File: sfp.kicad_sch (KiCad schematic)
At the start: 33 parts, among them J12 Bel-Fuse_SFP+_1x20_SS-79100-0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

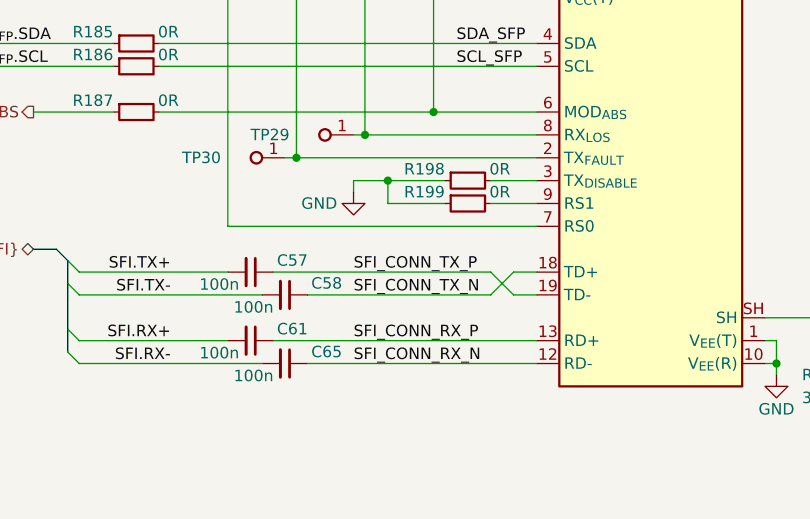
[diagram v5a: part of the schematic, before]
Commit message: [#85326] Update SFP connection
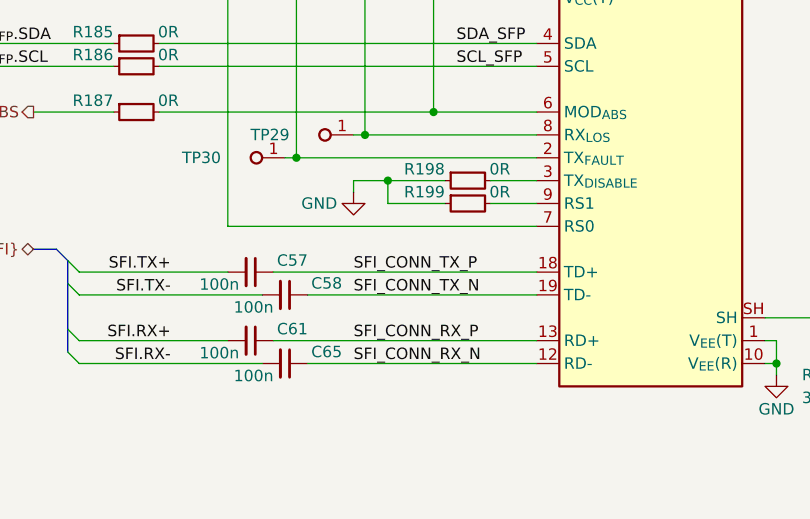
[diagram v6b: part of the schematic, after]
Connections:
- net SFI_CONN_TX_N: now also J12.19 (TD-); no longer J12.18 (TD+)
- net SFI_CONN_TX_P: now also J12.18 (TD+); no longer J12.19 (TD-)
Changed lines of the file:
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@@
-	(wire
-		(pts
-			(xy 182.88 151.13) (xy 185.42 151.13)
-		)
-		(stroke
-			(width 0)
-			(type default)
-		)
-	)
 	(wire
 		(pts
@@
 	(wire
 		(pts
-			(xy 182.88 153.67) (xy 185.42 153.67)
-		)
-		(stroke
-			(width 0)
-			(type default)
-		)
-	)
-	(wire
-		(pts
 			(xy 287.02 156.21) (xy 287.02 161.29)
 		)
@@
 	(wire
 		(pts
-			(xy 156.21 151.13) (xy 180.34 151.13)
+			(xy 156.21 151.13) (xy 185.42 151.13)
 		)
 		(stroke
@@
 	(wire
 		(pts
-			(xy 180.34 153.67) (xy 182.88 151.13)
-		)
-		(stroke
-			(width 0)
-			(type default)
-		)
-	)
-	(wire
-		(pts
 			(xy 246.38 127) (xy 246.38 128.27)
 		)
@@
 	(wire
 		(pts
-			(xy 160.02 153.67) (xy 180.34 153.67)
+			(xy 160.02 153.67) (xy 185.42 153.67)
 		)
 		(stroke
@@
 		)
 		(stroke
-			(width 0)
-			(type default)
-		)
-	)
-	(wire
-		(pts
-			(xy 180.34 151.13) (xy 182.88 153.67)
-		)
-		(stroke

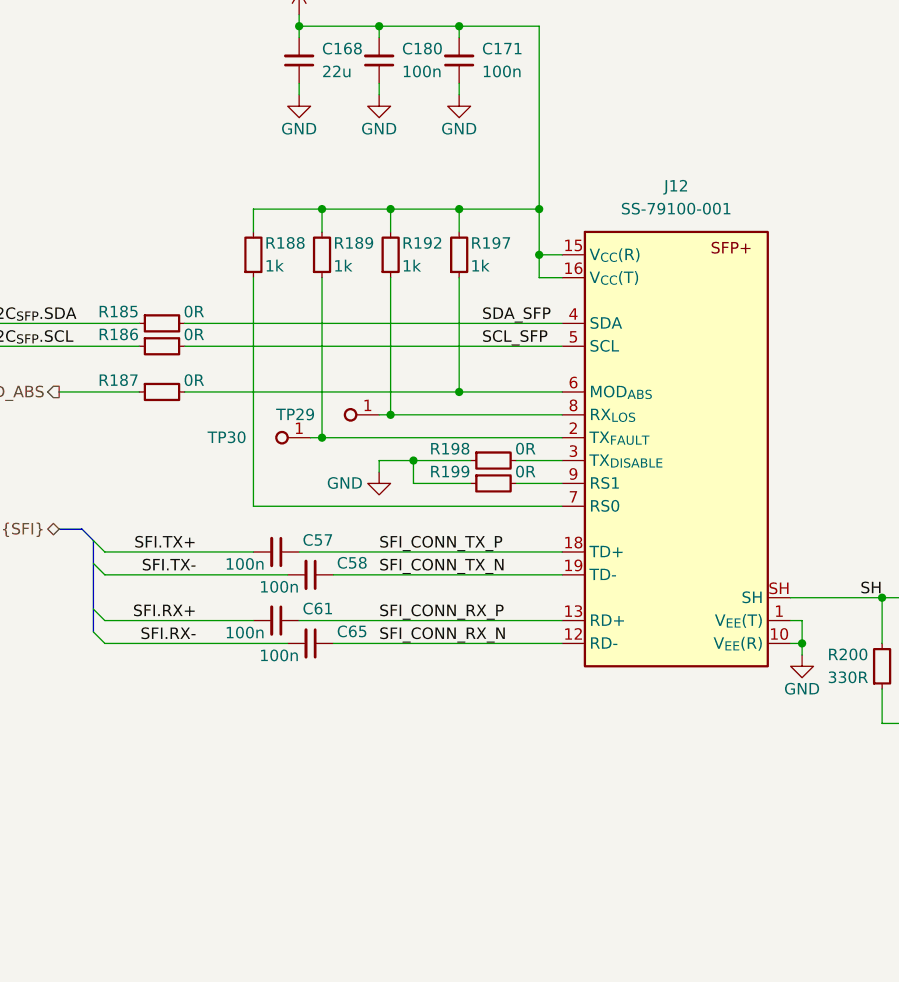
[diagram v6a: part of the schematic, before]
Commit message: [#85326] Fix incorrect GPIO voltage levels, add SFP related TVS
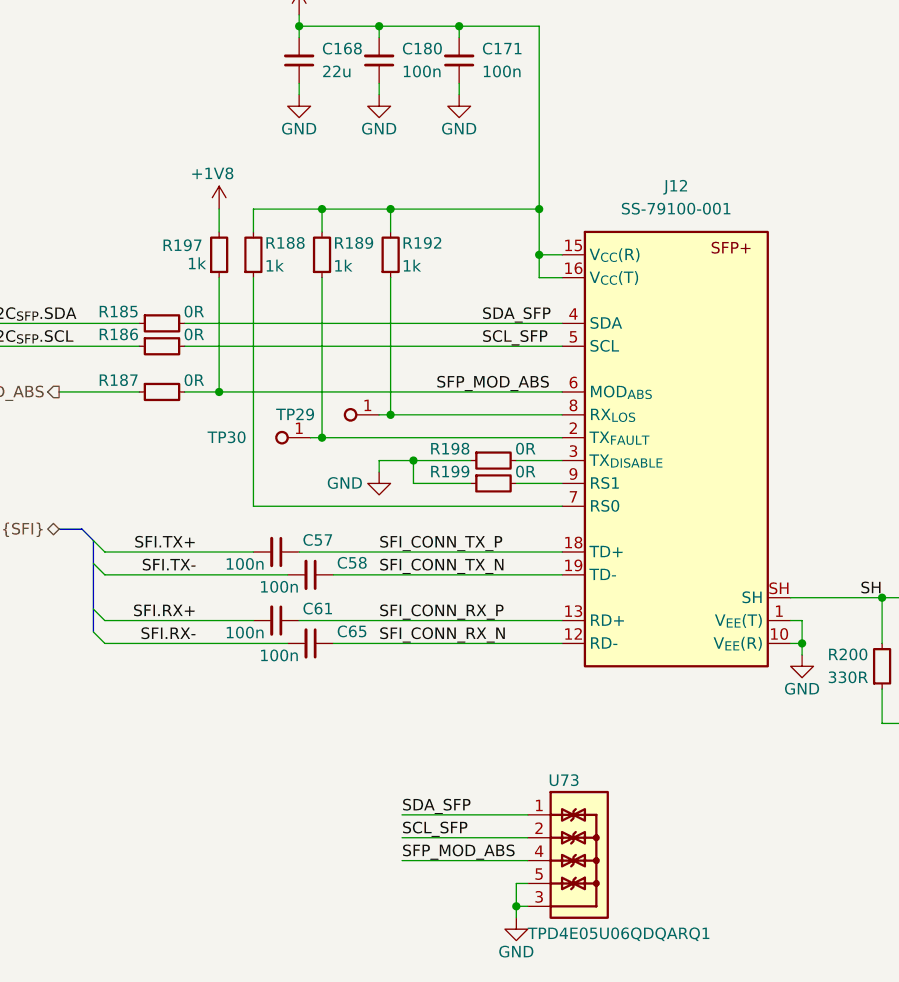
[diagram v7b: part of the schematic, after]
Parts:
- added U73: TPD4E05U06QDQARQ1, antmicro-footprints:USON-10_2.5x1mm_P0.5mm, symbol antmicroTVSDiodes:TPD4E05U06QDQARQ1
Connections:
- net +3V3: no longer R197.2
- net GND: now also U73.3, U73.5, U73.6, U73.8
- net SCL_SFP: now also U73.2, U73.9
- net SDA_SFP: now also U73.1, U73.10
- net SFP_MOD_ABS: now reaches J12.6 (MOD_{ABS}), R187.2, R197.1
- net SFP_MOD_ABS: now also U73.4, U73.7
- new net +1V8: R197.2
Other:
- moved on the sheet: R197

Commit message: [#85488] Annotate sch
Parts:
- C57, C58, C61, C65: value C_100n_0402 -> C_100n_0201; footprint antmicro-footprints:C_0402_1005Metric -> antmicro-footprints:C_0201; symbol antmicroCapacitors0402:C_100n_0402 -> antmicroCapacitorsmisc:C_100n_0201; MPN GRM155R61H104KE14D -> CC0201KRX6S5BB104; Manufacturer Murata -> YAGEO; Public (none) -> False
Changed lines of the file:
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@@
 	(title_block
 		(title "Jetson AGX Thor Baseboard")
-		(date "2025-10-16")
+		(date "2025-10-21")
 		(rev "1.0.0")
 		(company "Antmicro Ltd")
@@
 	)
 	(symbol
-		(lib_id "antmicroCapacitors0402:C_100n_0402")
+		(lib_id "antmicroCapacitorsmisc:C_100n_0201")
 		(at 156.21 158.75 180)
 		(unit 1)
@@
 			)
 		)
-		(property "Value" "C_100n_0402"
+		(property "Value" "C_100n_0201"
 			(at 135.89 148.59 0)
 			(effects
@@
 			)
 		)
-		(property "Footprint" "antmicro-footprints:C_0402_1005Metric"
+		(property "Footprint" "antmicro-footprints:C_0201"
 			(at 135.89 146.05 0)
 			(effects
@@
 			)
 		)
-		(property "Datasheet" "https://www.murata.com/products/productdetail?partno=GRM155R61H104KE14%23"
+		(property "Datasheet" "https://www.yageo.com/en/Chart/Download/pdf/CC0201KRX6S5BB104"
 			(at 135.89 143.51 0)
 			(effects
@@
 			)
 		)
-		(property "Description" "SMD Multilayer Ceramic Capacitor, 0.1 µF, 50 V, 0402 [1005 Metric], ± 10%, X5R, GRM Series"
+		(property "Description" "SMD Multilayer Ceramic Capacitor, 0.1 µF, 6.3 V, 0201 [0603 Metric], ± 10%, X6S, CC Series"
 			(at 156.21 158.75 0)
 			(effects
@@
 			)
 		)
-		(property "Manufacturer" "Murata"
+		(property "Manufacturer" "YAGEO"
 			(at 135.89 138.43 0)
 			(effects
@@
 			)
 		)
-		(property "MPN" "GRM155R61H104KE14D"
+		(property "MPN" "CC0201KRX6S5BB104"
 			(at 135.89 140.97 0)
 			(effects
@@
 			)
 		)
+		(property "Public" "False"
+			(at 135.89 125.73 0)
+			(effects
+				(font
+					(size 1.27 1.27)
+				)
+				(justify left bottom)
+				(hide yes)
+			)
+		)
 		(pin "1"
 		)
@@
 	)
 	(symbol
-		(lib_id "antmicroCapacitors0402:C_100n_0402")
+		(lib_id "antmicroCapacitorsmisc:C_100n_0201")
 		(at 160.02 161.29 180)
 		(unit 1)
@@
 			)
 		)
-		(property "Value" "C_100n_0402"
+		(property "Value" "C_100n_0201"
 			(at 139.7 151.13 0)
 			(effects
@@
 			)
 		)
-		(property "Footprint" "antmicro-footprints:C_0402_1005Metric"
+		(property "Footprint" "antmicro-footprints:C_0201"
 			(at 139.7 148.59 0)
 			(effects
@@
 			)
 		)
-		(property "Datasheet" "https://www.murata.com/products/productdetail?partno=GRM155R61H104KE14%23"
+		(property "Datasheet" "https://www.yageo.com/en/Chart/Download/pdf/CC0201KRX6S5BB104"
 			(at 139.7 146.05 0)
 			(effects
@@
 			)
 		)
-		(property "Description" "SMD Multilayer Ceramic Capacitor, 0.1 µF, 50 V, 0402 [1005 Metric], ± 10%, X5R, GRM Series"
+		(property "Description" "SMD Multilayer Ceramic Capacitor, 0.1 µF, 6.3 V, 0201 [0603 Metric], ± 10%, X6S, CC Series"
 			(at 160.02 161.29 0)
 			(effects
@@
 			)
 		)
-		(property "Manufacturer" "Murata"
+		(property "Manufacturer" "YAGEO"
 			(at 139.7 140.97 0)
 			(effects
@@
 			)
 		)
-		(property "MPN" "GRM155R61H104KE14D"
+		(property "MPN" "CC0201KRX6S5BB104"
 			(at 139.7 143.51 0)
 			(effects
@@
 			)
 		)
+		(property "Public" "False"
+			(at 139.7 128.27 0)
+			(effects
+				(font
+					(size 1.27 1.27)
+				)
+				(justify left bottom)
+				(hide yes)
+			)
+		)
 		(pin "1"
 		)
@@
 	)
 	(symbol
-		(lib_id "antmicroCapacitors0402:C_100n_0402")
+		(lib_id "antmicroCapacitorsmisc:C_100n_0201")
 		(at 156.21 151.13 180)
 		(unit 1)
@@
 			)
 		)
-		(property "Value" "C_100n_0402"
+		(property "Value" "C_100n_0201"
 			(at 135.89 140.97 0)
 			(effects
@@
 			)
 		)
-		(property "Footprint" "antmicro-footprints:C_0402_1005Metric"
+		(property "Footprint" "antmicro-footprints:C_0201"
 			(at 135.89 138.43 0)
 			(effects
@@
 			)
 		)
-		(property "Datasheet" "https://www.murata.com/products/productdetail?partno=GRM155R61H104KE14%23"
+		(property "Datasheet" "https://www.yageo.com/en/Chart/Download/pdf/CC0201KRX6S5BB104"
 			(at 135.89 135.89 0)
 			(effects
@@
 			)
 		)
-		(property "Description" "SMD Multilayer Ceramic Capacitor, 0.1 µF, 50 V, 0402 [1005 Metric], ± 10%, X5R, GRM Series"
+		(property "Description" "SMD Multilayer Ceramic Capacitor, 0.1 µF, 6.3 V, 0201 [0603 Metric], ± 10%, X6S, CC Series"
 			(at 156.21 151.13 0)
 			(effects
@@
 			)
 		)
-		(property "Manufacturer" "Murata"
+		(property "Manufacturer" "YAGEO"
 			(at 135.89 130.81 0)
 			(effects
@@
 			)
 		)
-		(property "MPN" "GRM155R61H104KE14D"
+		(property "MPN" "CC0201KRX6S5BB104"
 			(at 135.89 133.35 0)
 			(effects
@@
 			)
 		)
+		(property "Public" "False"
+			(at 135.89 118.11 0)
+			(effects
+				(font
+					(size 1.27 1.27)
+				)
+				(justify left bottom)
+				(hide yes)
+			)
+		)
 		(pin "1"
 		)
@@
 	)
 	(symbol
-		(lib_id "antmicroCapacitors0402:C_100n_0402")
+		(lib_id "antmicroCapacitorsmisc:C_100n_0201")
 		(at 160.02 153.67 180)
 		(unit 1)
@@
 			)
 		)
-		(property "Value" "C_100n_0402"
+		(property "Value" "C_100n_0201"
 			(at 139.7 143.51 0)
 			(effects
@@
 			)
 		)
-		(property "Footprint" "antmicro-footprints:C_0402_1005Metric"
+		(property "Footprint" "antmicro-footprints:C_0201"
 			(at 139.7 140.97 0)
 			(effects
@@
 			)
 		)
-		(property "Datasheet" "https://www.murata.com/products/productdetail?partno=GRM155R61H104KE14%23"
+		(property "Datasheet" "https://www.yageo.com/en/Chart/Download/pdf/CC0201KRX6S5BB104"
 			(at 139.7 138.43 0)
 			(effects
@@
 			)
 		)
-		(property "Description" "SMD Multilayer Ceramic Capacitor, 0.1 µF, 50 V, 0402 [1005 Metric], ± 10%, X5R, GRM Series"
+		(property "Description" "SMD Multilayer Ceramic Capacitor, 0.1 µF, 6.3 V, 0201 [0603 Metric], ± 10%, X6S, CC Series"
 			(at 160.02 153.67 0)
 			(effects
@@
 			)
 		)
-		(property "Manufacturer" "Murata"
+		(property "Manufacturer" "YAGEO"
 			(at 139.7 133.35 0)
 			(effects
@@
 			)
 		)
-		(property "MPN" "GRM155R61H104KE14D"
+		(property "MPN" "CC0201KRX6S5BB104"
 			(at 139.7 135.89 0)
 			(effects
@@
 			(effects
 				(font
+					(size 1.27 1.27)
+				)
+				(justify left bottom)
+				(hide yes)
+			)
+		)
+		(property "Public" "False"
+			(at 139.7 120.65 0)
+			(effects
+				(font
